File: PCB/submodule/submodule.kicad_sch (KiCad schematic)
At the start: 0 parts

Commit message: Power supply & TPDs
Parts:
- added C23, C24, C25, C27: 2.2uF, symbol Device:C
- added C26: 10uF, symbol Device:C
- added C28: 0.01uF, symbol Device:C
- added J22: Conn_01x03, symbol Connector_Generic:Conn_01x05
- added J24: Conn_02x07_Odd_Even, symbol Connector_Generic:Conn_02x07_Odd_Even
- added J32, J33, J35, J36, J37, J38, J39, J40, J41, J42: Conn_Coaxial, Connector_Coaxial:U.FL_Molex_MCRF_73412-0110_Vertical, symbol Connector:Conn_Coaxial
- added J34: ELECT_AUX, symbol Connector_Generic:Conn_01x12
- added JP16: SB_GND_TIE, symbol Jumper:SolderJumper_2_Open
- added U6: LP5907, DBV0005A_N, symbol Power_LDO:LP5907MFX-2.5_NOPB
- added U7: TPS72325, DBV0005A_N, symbol Power_LDO:TPS72325QDBVRQ1
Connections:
- new net: C28.1, U7.4 (NR)
- new net +3.3V: C23.1, J24.1 (Pin_1), U6.1 (VIN), U6.3 (EN)
- new net -3V3: C27.1, J24.2 (Pin_2), U7.2 (IN), U7.3 (EN)
- new net AGND: C23.2, C24.2, C25.2, C26.2, C27.2, C28.2, J24.12 (Pin_12), J33.2 (Ext), J34.11 (Pin_11), J34.12 (Pin_12), JP16.2 (B), U6.2 (GND), U7.1 (GND)
- new net AVDD: C24.1, U6.5 (VOUT)
- new net AVSS: C25.1, C26.1, U7.5 (OUT)
- new net BIAS_ELEC: J33.1 (In), J34.10 (Pin_10)
- new net BIAS_SHD: J32.2 (Ext), J36.2 (Ext), J37.2 (Ext), J38.2 (Ext), J40.2 (Ext), J41.2 (Ext), J42.2 (Ext)
- new net CH1_IN: J34.1 (Pin_1)
- new net CH2_IN: J34.2 (Pin_2)
- new net CH3_IN: J34.3 (Pin_3)
- new net CH4_IN: J34.4 (Pin_4)
- new net CH5_IN: J34.5 (Pin_5)
- new net CH6_IN: J34.6 (Pin_6)
- new net CH7_IN: J34.7 (Pin_7)
- new net CH8_IN: J34.8 (Pin_8)
- new net CH_IN1: J35.1 (In)
- new net CH_IN2: J36.1 (In)
- new net CH_IN3: J37.1 (In)
- new net CH_IN4: J38.1 (In)
- new net CH_IN5: J39.1 (In)
- new net CH_IN6: J40.1 (In)
- new net CH_IN7: J41.1 (In)
- new net CH_IN8: J42.1 (In)
- new net CS: J24.3 (Pin_3)
- new net DGND: J24.11 (Pin_11), J24.13 (Pin_13), J24.14 (Pin_14), JP16.1 (A)
- new net DRDY_OUT: J24.4 (Pin_4)
- new net IN_ELEC: J32.1 (In), J34.9 (Pin_9)
- new net MISO: J24.9 (Pin_9)
- new net MOSI: J24.7 (Pin_7)
- new net PWDN: J24.10 (Pin_10)
- new net RESET: J24.6 (Pin_6)
- new net SCLK: J24.5 (Pin_5)
- new net START: J24.8 (Pin_8)
- no-connect marks 0 -> 1
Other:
- sheet ADS1299 ports: added GPIO1, GPIO2, GPIO3, GPIO4, PWDN, RESET, SCLK, START; removed IN1-, IN2-, IN3-, IN4-, IN5-, IN6-, IN7-, IN8-, SLCK
- sheet PROTECCIONES ports: added BIAS_ELEC, CH_IN[1..8], IN_ELEC; removed none
- note added: "+2.5V"
- note added: "-2.5V"
- note added: "AGREAR DGND al micro"
- note added: "CONECTOR A MICRO"

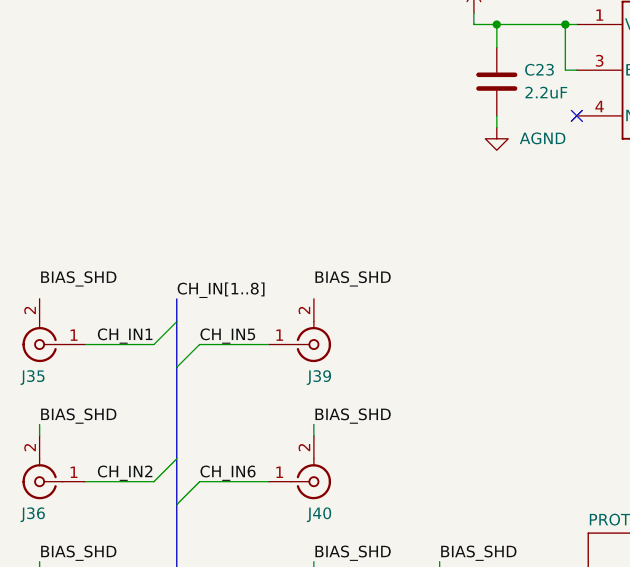
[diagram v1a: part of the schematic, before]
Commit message: draft initial wiring for submodule (pending pin check)
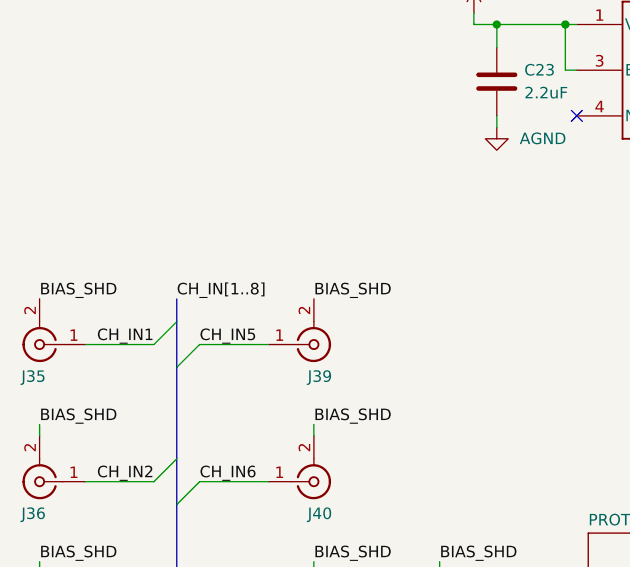
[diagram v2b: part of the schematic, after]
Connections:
- net BIAS_SHD: now also J35.2 (Ext), J39.2 (Ext)
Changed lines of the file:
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@@
 	)
 	(label "BIAS_SHD"
-		(at 66.04 59.69 0)
+		(at 66.04 60.96 0)
 		(effects
 			(font
@@
 	)
 	(label "BIAS_SHD"
-		(at 35.56 59.69 0)
+		(at 35.56 60.96 0)
 		(effects
 			(font

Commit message: fix GPIOs
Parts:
- removed J22: Conn_01x03, symbol Connector_Generic:Conn_01x05
- added J6: GPIOs, symbol Connector_Generic:Conn_01x04
- J24: value Conn_02x07_Odd_Even -> MAIN
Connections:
- net ADS1299/GPIO1: now also J6.1 (Pin_1)
- net ADS1299/GPIO2: now also J6.2 (Pin_2)
- net ADS1299/GPIO3: now also J6.3 (Pin_3)
- net ADS1299/GPIO4: now also J6.4 (Pin_4)
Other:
- note removed: "AGREAR DGND al micro"
- note removed: "CONECTOR A MICRO"
- moved on the sheet: J34

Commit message: fix BIAS (pending ERC & footprints)
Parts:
- added J13: CONN_SUBMODULES, symbol Connector_Generic:Conn_02x09_Odd_Even
- added J9: Conn_01x06, symbol Connector_Generic:Conn_01x08
- added TP1: TestPoint, symbol Connector:TestPoint
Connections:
- net CH1_IN is gone; now on net CH_IN1: J34.1 (Pin_1)
- net CH2_IN is gone; now on net CH_IN2: J34.2 (Pin_2)
- net CH3_IN is gone; now on net CH_IN3: J34.3 (Pin_3)
- net CH4_IN is gone; now on net CH_IN4: J34.4 (Pin_4)
- net CH5_IN is gone; now on net CH_IN5: J34.5 (Pin_5)
- net CH6_IN is gone; now on net CH_IN6: J34.6 (Pin_6)
- net CH7_IN is gone; now on net CH_IN7: J34.7 (Pin_7)
- net CH8_IN is gone; now on net CH_IN8: J34.8 (Pin_8)
- net +3.3V: now also J13.2 (Pin_2), J9.5 (Pin_5), J9.7 (Pin_7)
- net -3V3: now also J9.6 (Pin_6)
- net AGND: now also J13.11 (Pin_11), J13.7 (Pin_7), J9.1 (Pin_1)
- net AVDD: now also J13.1 (Pin_1), J9.2 (Pin_2)
- net AVSS: now also J13.3 (Pin_3), J9.3 (Pin_3)
- net CS: now also J13.12 (Pin_12)
- net DGND: now also J13.10 (Pin_10), J13.13 (Pin_13), J13.17 (Pin_17), J9.4 (Pin_4), J9.8 (Pin_8)
- net MOSI: now also J13.6 (Pin_6)
- net PWDN: now also J13.18 (Pin_18)
- net RESET: now also J13.16 (Pin_16)
- net SCLK: now also J13.8 (Pin_8)
- net START: now also J13.14 (Pin_14)
- new net BIASINV_LINK: J13.5 (Pin_5)
- new net CLK: J13.15 (Pin_15)
- new net DAISY_OUT_LINK: J13.4 (Pin_4)
- new net SRB1_LINK: J13.9 (Pin_9)
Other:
- note added: "Debug Access"
- moved on the sheet: J24, JP16
